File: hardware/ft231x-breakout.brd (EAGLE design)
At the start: 24.1 x 15.2 mm, 25 parts, among them Q1 2N7002PW, U1 FT231XS, X1 USB-MICROB

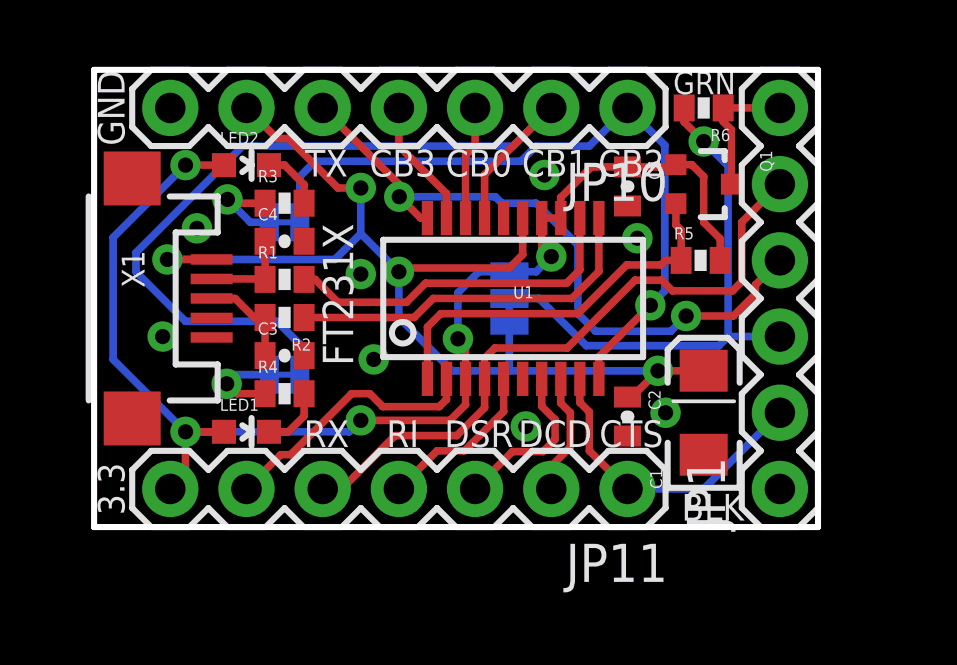
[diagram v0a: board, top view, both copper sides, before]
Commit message: Updated micro USB connector
This is Pete's micro-USB package, which has two more pads under the
connector to solidify the physical connection.
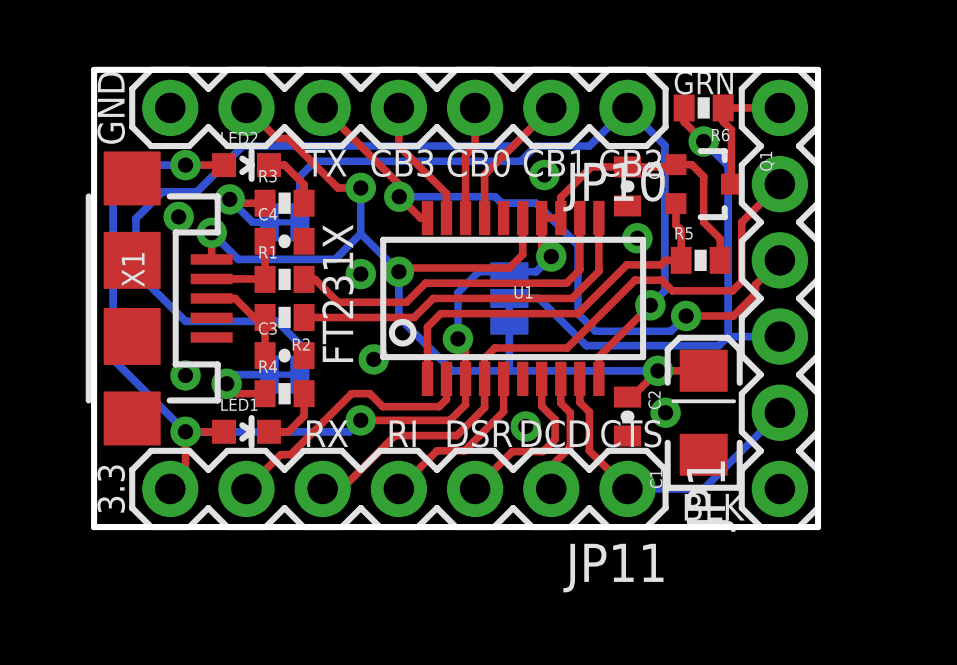
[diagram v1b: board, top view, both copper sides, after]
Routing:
- net VCC: track 37.4 -> 35.7 mm
- net 3.3V: track 43.9 -> 44.6 mm
- net RXLED: track 28.5 -> 29.2 mm
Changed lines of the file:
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@@
 <setting verticaltext="up"/>
 </settings>
-<grid distance="0.05" unitdist="inch" unit="inch" style="lines" multiple="1" display="yes" altdistance="0.005" altunitdist="inch" altunit="inch"/>
+<grid distance="0.05" unitdist="inch" unit="inch" style="lines" multiple="1" display="yes" altdistance="0.001" altunitdist="inch" altunit="inch"/>
 <layers>
 <layer number="1" name="Top" color="4" fill="1" visible="yes" active="yes"/>
@@
 <layer number="27" name="tValues" color="7" fill="1" visible="no" active="yes"/>
 <layer number="28" name="bValues" color="7" fill="1" visible="no" active="yes"/>
-<layer number="29" name="tStop" color="7" fill="3" visible="no" active="yes"/>
-<layer number="30" name="bStop" color="7" fill="6" visible="no" active="yes"/>
+<layer number="29" name="tStop" color="7" fill="3" visible="yes" active="yes"/>
+<layer number="30" name="bStop" color="7" fill="6" visible="yes" active="yes"/>
 <layer number="31" name="tCream" color="7" fill="4" visible="no" active="yes"/>
 <layer number="32" name="bCream" color="7" fill="5" visible="no" active="yes"/>
@@
 <layer number="220" name="220bmp" color="21" fill="1" visible="no" active="no"/>
 <layer number="221" name="221bmp" color="22" fill="1" visible="no" active="no"/>
+<layer number="222" name="222bmp" color="23" fill="1" visible="no" active="no"/>
 <layer number="223" name="223bmp" color="24" fill="1" visible="no" active="no"/>
 <layer number="224" name="224bmp" color="25" fill="1" visible="no" active="no"/>
@@
 <via x="14.3891" y="3.3528" extent="1-16" drill="0.508"/>
 <via x="9.3218" y="5.588" extent="1-16" drill="0.508"/>
-<via x="2.286" y="6.35" extent="1-16" drill="0.508"/>
-<via x="3.429" y="9.9568" extent="1-16" drill="0.508"/>
+<via x="3.048" y="5.0546" extent="1-16" drill="0.508"/>
+<via x="2.8194" y="10.3378" extent="1-16" drill="0.508"/>
 <via x="8.89" y="8.4328" extent="1-16" drill="0.508"/>
 <contactref element="JP10" pad="7"/>
@@
 <wire x1="14.2875" y1="10.2997" x2="14.2875" y2="9.0805" width="0.254" layer="1"/>
 <contactref element="X1" pad="VBUS"/>
-<wire x1="3.92" y1="8.92" x2="2.443" y2="8.92" width="0.254" layer="1"/>
-<via x="2.443" y="8.92" extent="1-16" drill="0.508"/>
+<wire x1="3.92" y1="8.92" x2="3.92" y2="9.809" width="0.254" layer="1"/>
+<via x="3.92" y="9.809" extent="1-16" drill="0.508"/>
 <via x="10.16" y="8.509" extent="1-16" drill="0.508"/>
 <contactref element="JP10" pad="6"/>
@@
 <wire x1="18.796" y1="5.207" x2="20.317" y2="5.207" width="0.254" layer="1"/>
 <wire x1="20.317" y1="5.207" x2="20.32" y2="5.21" width="0.254" layer="1"/>
-<wire x1="2.443" y1="8.92" x2="8.031" y2="8.92" width="0.254" layer="16"/>
 <wire x1="18.796" y1="5.207" x2="13.843" y2="5.207" width="0.254" layer="16"/>
 <wire x1="13.843" y1="5.207" x2="11.938" y2="5.207" width="0.254" layer="16"/>
@@
 <wire x1="10.287" y1="8.636" x2="10.16" y2="8.509" width="0.254" layer="1"/>
 <wire x1="8.89" y1="9.779" x2="10.16" y2="8.509" width="0.254" layer="16"/>
+<wire x1="3.92" y1="9.809" x2="4.809" y2="8.92" width="0.254" layer="16"/>
+<wire x1="4.809" y1="8.92" x2="8.031" y2="8.92" width="0.254" layer="16"/>
 </signal>
 <signal name="CTS">
@@
 <contactref element="LED1" pad="A"/>
 <via x="3.048" y="3.175" extent="1-16" drill="0.508"/>
-<wire x1="0.635" y1="5.588" x2="0.635" y2="9.652" width="0.254" layer="16"/>
+<wire x1="0.635" y1="5.588" x2="0.635" y2="10.922" width="0.254" layer="16"/>
 <via x="8.89" y="3.556" extent="1-16" drill="0.508"/>
 <wire x1="8.89" y1="3.556" x2="11.8618" y2="3.556" width="0.254" layer="1"/>
@@
 <wire x1="4.33" y1="12.065" x2="3.048" y2="12.065" width="0.254" layer="1"/>
 <via x="3.048" y="12.065" extent="1-16" drill="0.508"/>
-<wire x1="3.048" y1="12.065" x2="0.635" y2="9.652" width="0.254" layer="16"/>
 <contactref element="R5" pad="2"/>
 <contactref element="Q1" pad="1"/>
@@
 <wire x1="3.048" y1="3.175" x2="3.048" y2="1.778" width="0.254" layer="1"/>
 <wire x1="3.048" y1="1.778" x2="2.54" y2="1.27" width="0.254" layer="1"/>
+<wire x1="3.048" y1="12.065" x2="1.778" y2="12.065" width="0.254" layer="16"/>
+<wire x1="1.778" y1="12.065" x2="0.635" y2="10.922" width="0.254" layer="16"/>
 </signal>
 <signal name="CBUS3">
@@
 <wire x1="6.096" y1="6.858" x2="3.048" y2="6.858" width="0.254" layer="16"/>
 <wire x1="3.048" y1="6.858" x2="1.397" y2="8.509" width="0.254" layer="16"/>
-<wire x1="1.397" y1="8.509" x2="1.397" y2="9.144" width="0.254" layer="16"/>
-<wire x1="1.397" y1="9.144" x2="4.953" y2="12.7" width="0.254" layer="16"/>
 <wire x1="4.953" y1="12.7" x2="13.97" y2="12.7" width="0.254" layer="16"/>
 <wire x1="13.97" y1="12.7" x2="15.24" y2="13.97" width="0.254" layer="16"/>
+<wire x1="1.397" y1="8.509" x2="1.397" y2="10.287" width="0.254" layer="16"/>
+<wire x1="1.397" y1="10.287" x2="2.286" y2="11.176" width="0.254" layer="16"/>
+<wire x1="2.286" y1="11.176" x2="3.429" y2="11.176" width="0.254" layer="16"/>
+<wire x1="3.429" y1="11.176" x2="4.953" y2="12.7" width="0.254" layer="16"/>
 </signal>
 <signal name="CBUS0">
@@
 <contactref element="R3" pad="1"/>
 <contactref element="SJ2" pad="2"/>
-<via x="4.445" y="10.922" extent="1-16" drill="0.508"/>
-<wire x1="5.7" y1="10.795" x2="4.572" y2="10.795" width="0.254" layer="1"/>
-<wire x1="4.572" y1="10.795" x2="4.445" y2="10.922" width="0.254" layer="1"/>
-<wire x1="5.842" y1="10.16" x2="5.207" y2="10.16" width="0.254" layer="16"/>
-<wire x1="5.207" y1="10.16" x2="4.445" y2="10.922" width="0.254" layer="16"/>
+<via x="4.5212" y="10.922" extent="1-16" drill="0.508"/>
+<wire x1="5.7" y1="10.795" x2="4.6482" y2="10.795" width="0.254" layer="1"/>
+<wire x1="4.6482" y1="10.795" x2="4.5212" y2="10.922" width="0.254" layer="1"/>
+<wire x1="5.842" y1="10.16" x2="5.2832" y2="10.16" width="0.254" layer="16"/>
+<wire x1="5.2832" y1="10.16" x2="4.5212" y2="10.922" width="0.254" layer="16"/>
 </signal>
 <signal name="N$8">
@@
 </signal>
 </signals>
+<errors>
+</errors>
 </board>
 </drawing>

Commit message: Silkscreen fixes: no-silk headers, moved labels
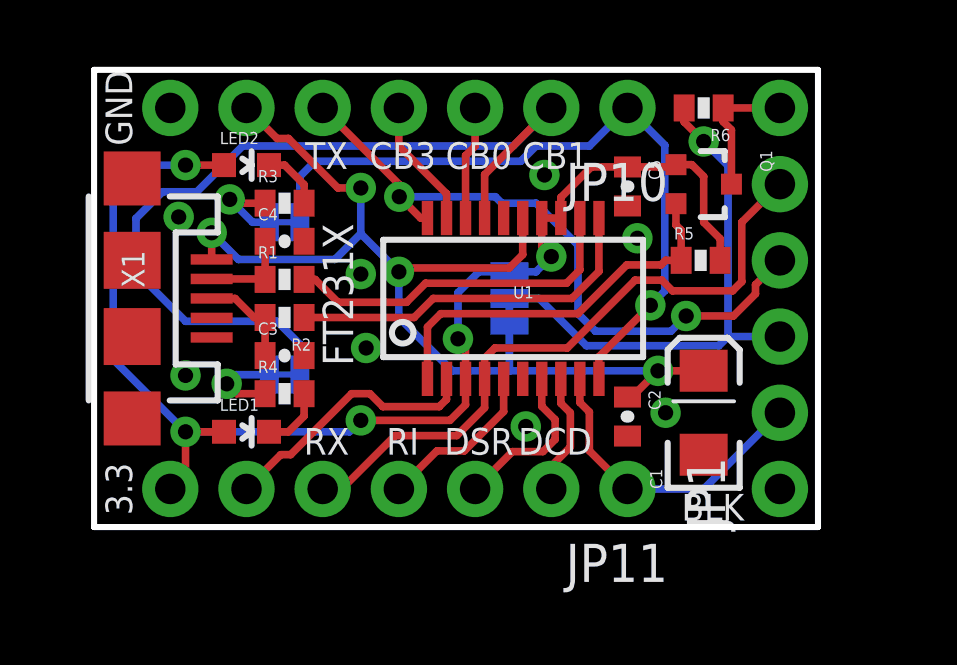
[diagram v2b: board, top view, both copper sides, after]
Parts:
- JP1: device SparkFun-Connectors:1X06 -> SparkFun-Connectors:1X06_NS
- JP10, JP11: device SparkFun-Connectors:1X07 -> SparkFun-Connectors:1X07_NS
- moved U$1 0.25 mm to (17.7, 7.62), turned to 0 degrees
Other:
- board text added: "DTR"
- board text removed: "GRN"
- board text removed: "RST"

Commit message: Added fiducials, minor silkscreen changes.
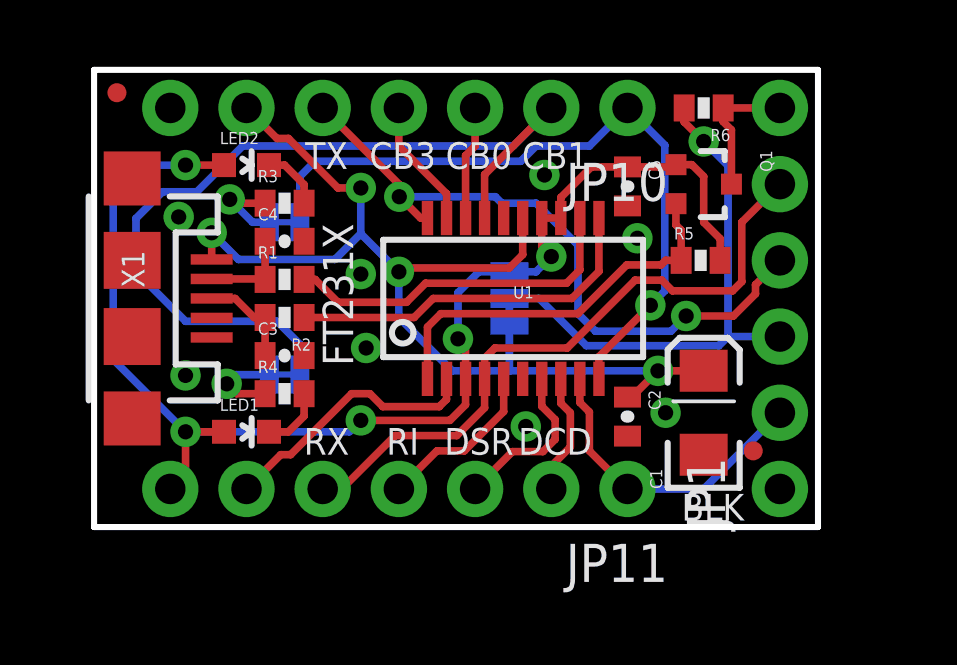
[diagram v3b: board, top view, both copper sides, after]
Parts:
- added JP3, JP4: FIDUCIALUFIDUCIAL, SparkFun-Aesthetics:MICRO-FIDUCIAL
- moved JP2 0.13 mm to (12.6, 5.84)
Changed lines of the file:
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@@
 <text x="15.367" y="11.938" size="0.889" layer="21" font="vector" ratio="15" rot="R180" align="top-center">CB1</text>
 <text x="7.747" y="11.938" size="0.889" layer="21" font="vector" ratio="15" rot="R180" align="top-center">TX</text>
-<text x="1.27" y="13.97" size="0.889" layer="21" font="vector" ratio="15" rot="R270" align="top-center">GND</text>
 <text x="15.367" y="3.302" size="0.889" layer="21" font="vector" ratio="15" rot="R180" align="bottom-center">DCD</text>
 <text x="12.827" y="3.302" size="0.889" layer="21" font="vector" ratio="15" rot="R180" align="bottom-center">DSR</text>
 <text x="10.287" y="3.302" size="0.889" layer="21" font="vector" ratio="15" rot="R180" align="bottom-center">RI</text>
 <text x="7.747" y="3.302" size="0.889" layer="21" font="vector" ratio="15" rot="R180" align="bottom-center">RX</text>
-<text x="1.27" y="1.27" size="0.889" layer="21" font="vector" ratio="15" rot="R90" align="bottom-center">3.3</text>
 <text x="7.62" y="7.747" size="1.016" layer="21" font="vector" ratio="15" rot="R90" align="top-center">FT231X</text>
 <text x="13.843" y="5.969" size="1.016" layer="22" font="vector" ratio="15" rot="MR0" align="top-center">5V</text>
@@
 <element name="R5" library="SparkFun-Passives" package="0402-RES" value="10k" x="20.2184" y="8.89"/>
 <element name="R6" library="SparkFun-Passives" package="0402-RES" value="10k" x="20.32" y="13.97" rot="R180"/>
-<element name="JP2" library="SparkFun-Aesthetics" package="SFE-NEW-WEB" value="LOGO-SFENW2" x="12.446" y="5.842" rot="MR0"/>
+<element name="JP2" library="SparkFun-Aesthetics" package="SFE-NEW-WEB" value="LOGO-SFENW2" x="12.573" y="5.842" rot="MR0"/>
 <element name="U$1" library="SparkFun-Aesthetics" package="OSHW-LOGO-S" value="OSHW-LOGOS" x="17.653" y="7.62" smashed="yes" rot="MR0"/>
+<element name="JP3" library="SparkFun-Aesthetics" package="MICRO-FIDUCIAL" value="FIDUCIALUFIDUCIAL" x="0.762" y="14.478"/>
+<element name="JP4" library="SparkFun-Aesthetics" package="MICRO-FIDUCIAL" value="FIDUCIALUFIDUCIAL" x="21.971" y="2.54"/>
 </elements>
 <signals>

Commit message: Production readiness
Created panel of boards. Adjusted fiducial position.
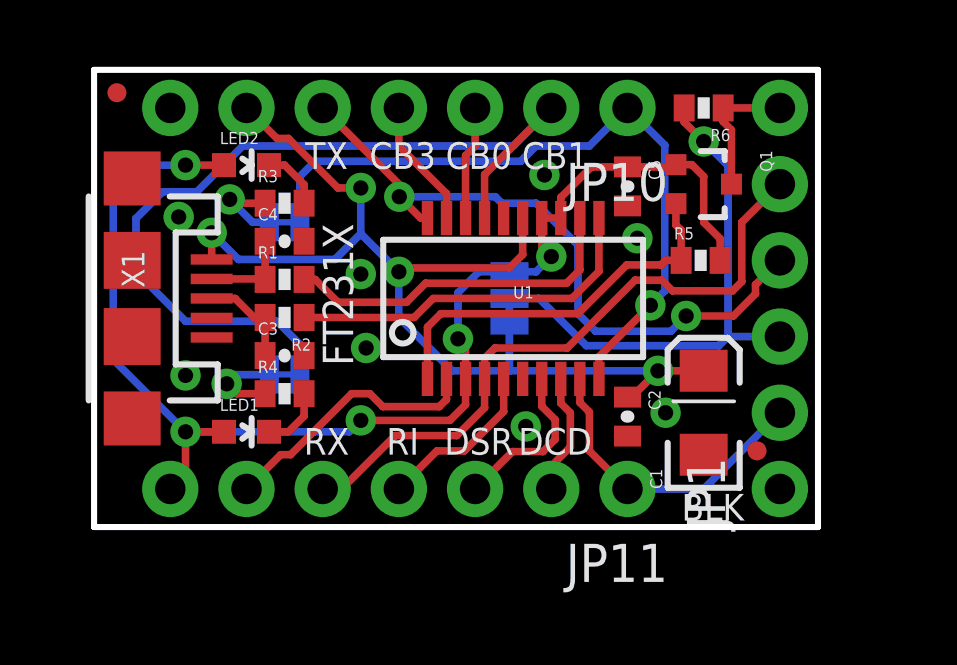
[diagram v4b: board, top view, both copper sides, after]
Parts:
- moved JP4 0.13 mm to (22.1, 2.54)
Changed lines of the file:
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@@
 <?xml version="1.0" encoding="utf-8"?>
 <!DOCTYPE eagle SYSTEM "eagle.dtd">
-<eagle version="6.4">
+<eagle version="6.3">
 <drawing>
 <settings>
@@
 <setting verticaltext="up"/>
 </settings>
-<grid distance="0.05" unitdist="inch" unit="inch" style="lines" multiple="1" display="yes" altdistance="0.005" altunitdist="inch" altunit="inch"/>
+<grid distance="0.05" unitdist="inch" unit="inch" style="lines" multiple="1" display="yes" altdistance="0.01" altunitdist="inch" altunit="inch"/>
 <layers>
 <layer number="1" name="Top" color="4" fill="1" visible="yes" active="yes"/>
@@
 <layer number="18" name="Vias" color="2" fill="1" visible="yes" active="yes"/>
 <layer number="19" name="Unrouted" color="6" fill="1" visible="yes" active="yes"/>
-<layer number="20" name="Dimension" color="15" fill="1" visible="yes" active="yes"/>
-<layer number="21" name="tPlace" color="16" fill="1" visible="yes" active="yes"/>
-<layer number="22" name="bPlace" color="14" fill="1" visible="yes" active="yes"/>
+<layer number="20" name="Dimension" color="6" fill="1" visible="yes" active="yes"/>
+<layer number="21" name="tPlace" color="6" fill="1" visible="yes" active="yes"/>
+<layer number="22" name="bPlace" color="6" fill="1" visible="yes" active="yes"/>
 <layer number="23" name="tOrigins" color="15" fill="1" visible="yes" active="yes"/>
 <layer number="24" name="bOrigins" color="15" fill="1" visible="yes" active="yes"/>
@@
 <layer number="47" name="Measures" color="7" fill="1" visible="no" active="yes"/>
 <layer number="48" name="Document" color="7" fill="1" visible="no" active="yes"/>
-<layer number="49" name="Reference" color="7" fill="1" visible="yes" active="yes"/>
+<layer number="49" name="Reference" color="7" fill="1" visible="no" active="yes"/>
 <layer number="50" name="dxf" color="7" fill="1" visible="no" active="no"/>
 <layer number="51" name="tDocu" color="6" fill="1" visible="yes" active="yes"/>
@@
 <element name="U$1" library="SparkFun-Aesthetics" package="OSHW-LOGO-S" value="OSHW-LOGOS" x="17.653" y="7.62" smashed="yes" rot="MR0"/>
 <element name="JP3" library="SparkFun-Aesthetics" package="MICRO-FIDUCIAL" value="FIDUCIALUFIDUCIAL" x="0.762" y="14.478"/>
-<element name="JP4" library="SparkFun-Aesthetics" package="MICRO-FIDUCIAL" value="FIDUCIALUFIDUCIAL" x="21.971" y="2.54"/>
+<element name="JP4" library="SparkFun-Aesthetics" package="MICRO-FIDUCIAL" value="FIDUCIALUFIDUCIAL" x="22.098" y="2.54"/>
 </elements>
 <signals>
@@
 </signal>
 </signals>
-<errors>
-</errors>
 </board>
 </drawing>

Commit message: Updated footprints, sch, microb
Updated to 0603 components
Updated to bossed microb
Trace reroutes
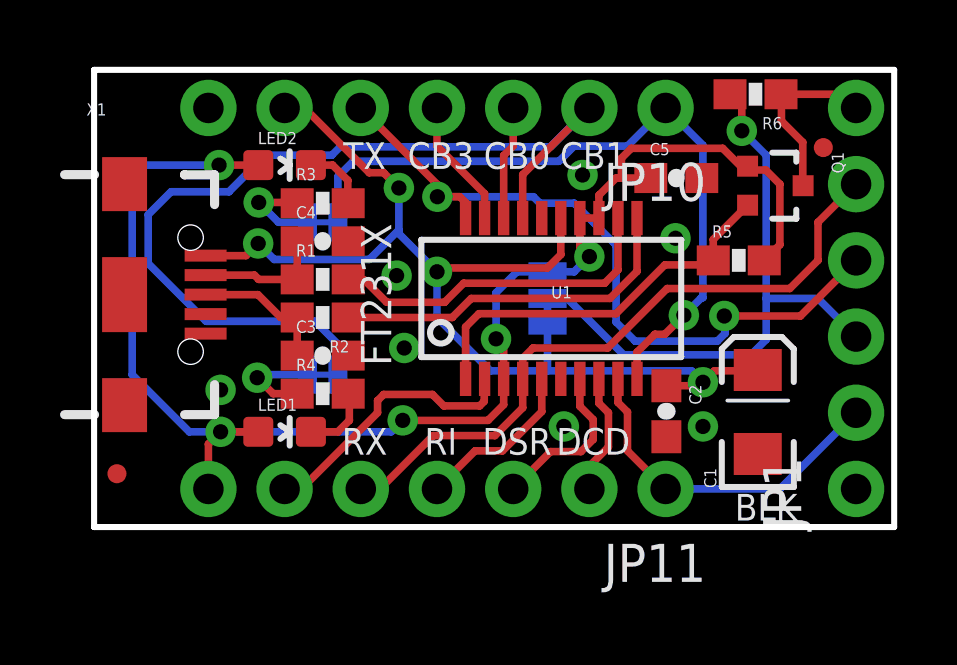
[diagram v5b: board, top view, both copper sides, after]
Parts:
- C2, C3, C4, C5: device SparkFun-Capacitors:0402-CAP -> SparkFun-Capacitors:0603-CAP
- R1, R2: device SparkFun-Resistors:0402-RES -> SparkFun-Resistors:0603-RES
- R3, R4, R5, R6: device SparkFun-Passives:0402-RES -> SparkFun-Resistors:0603-RES
- SJ3: device SparkFun-Passives:SJ_2S-TRACE -> SparkFun-Passives:PAD-JUMPER-2-NC_BY_TRACE_YES_SILK
- X1: value USB-MICROB -> (none); device SparkFun-Connectors:USB-MICROB -> SparkFun-Connectors:USB-AB-MICRO-SMD_V03
- moved JP3 12.7 mm to (0.76, 1.78)
- moved JP4 10.3 mm to (24.3, 12.6)
- moved JP1 2.54 mm to (25.4, 1.27)
- moved Q1 2.39 mm to (22.7, 11.4)
- moved C1 1.80 mm to (22.1, 3.84)
- moved R6 1.79 mm to (22.0, 14.4)
- moved U$1 1.66 mm to (19.3, 7.49)
- moved C5 1.65 mm to (19.4, 11.6), turned to 0 degrees
- moved C2 1.31 mm to (19.1, 3.86)
- moved C3 1.27 mm to (7.62, 5.71)
- moved C4 1.27 mm to (7.62, 9.53)
- moved R1 1.27 mm to (7.62, 8.26)
- moved R2 1.27 mm to (7.62, 6.99)
- moved R3 1.27 mm to (7.62, 10.8)
- moved R4 1.27 mm to (7.62, 4.45)
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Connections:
- net GND: now also X1.GND1; no longer X1.GND, X1.MT1, X1.MT2
- net N$3: now also X1.D+1; no longer X1.D+
- net N$4: now also X1.D-1; no longer X1.D-
- net VCC: now also X1.VBUS1; no longer X1.VBUS
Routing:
- net 3.3V: track 44.6 -> 49.5 mm
- net RXLED: track 29.2 -> 32.6 mm
- net VOUT: track 18.0 -> 20.5 mm
- net TXD: track 22.3 -> 24.5 mm
- net RESET: track 4.54 -> 6.04 mm
- net VCC: track 35.7 -> 37.1 mm
- net N$4: track 3.06 -> 4.38 mm
- net N$3: track 3.31 -> 4.64 mm
- net CTS: track 10.5 -> 11.7 mm
- net RXD: track 21.9 -> 22.4 mm
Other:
- board size 24.1 x 15.2 mm -> 26.7 x 15.2 mm
